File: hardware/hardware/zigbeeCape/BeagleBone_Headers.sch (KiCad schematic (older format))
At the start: 2 parts

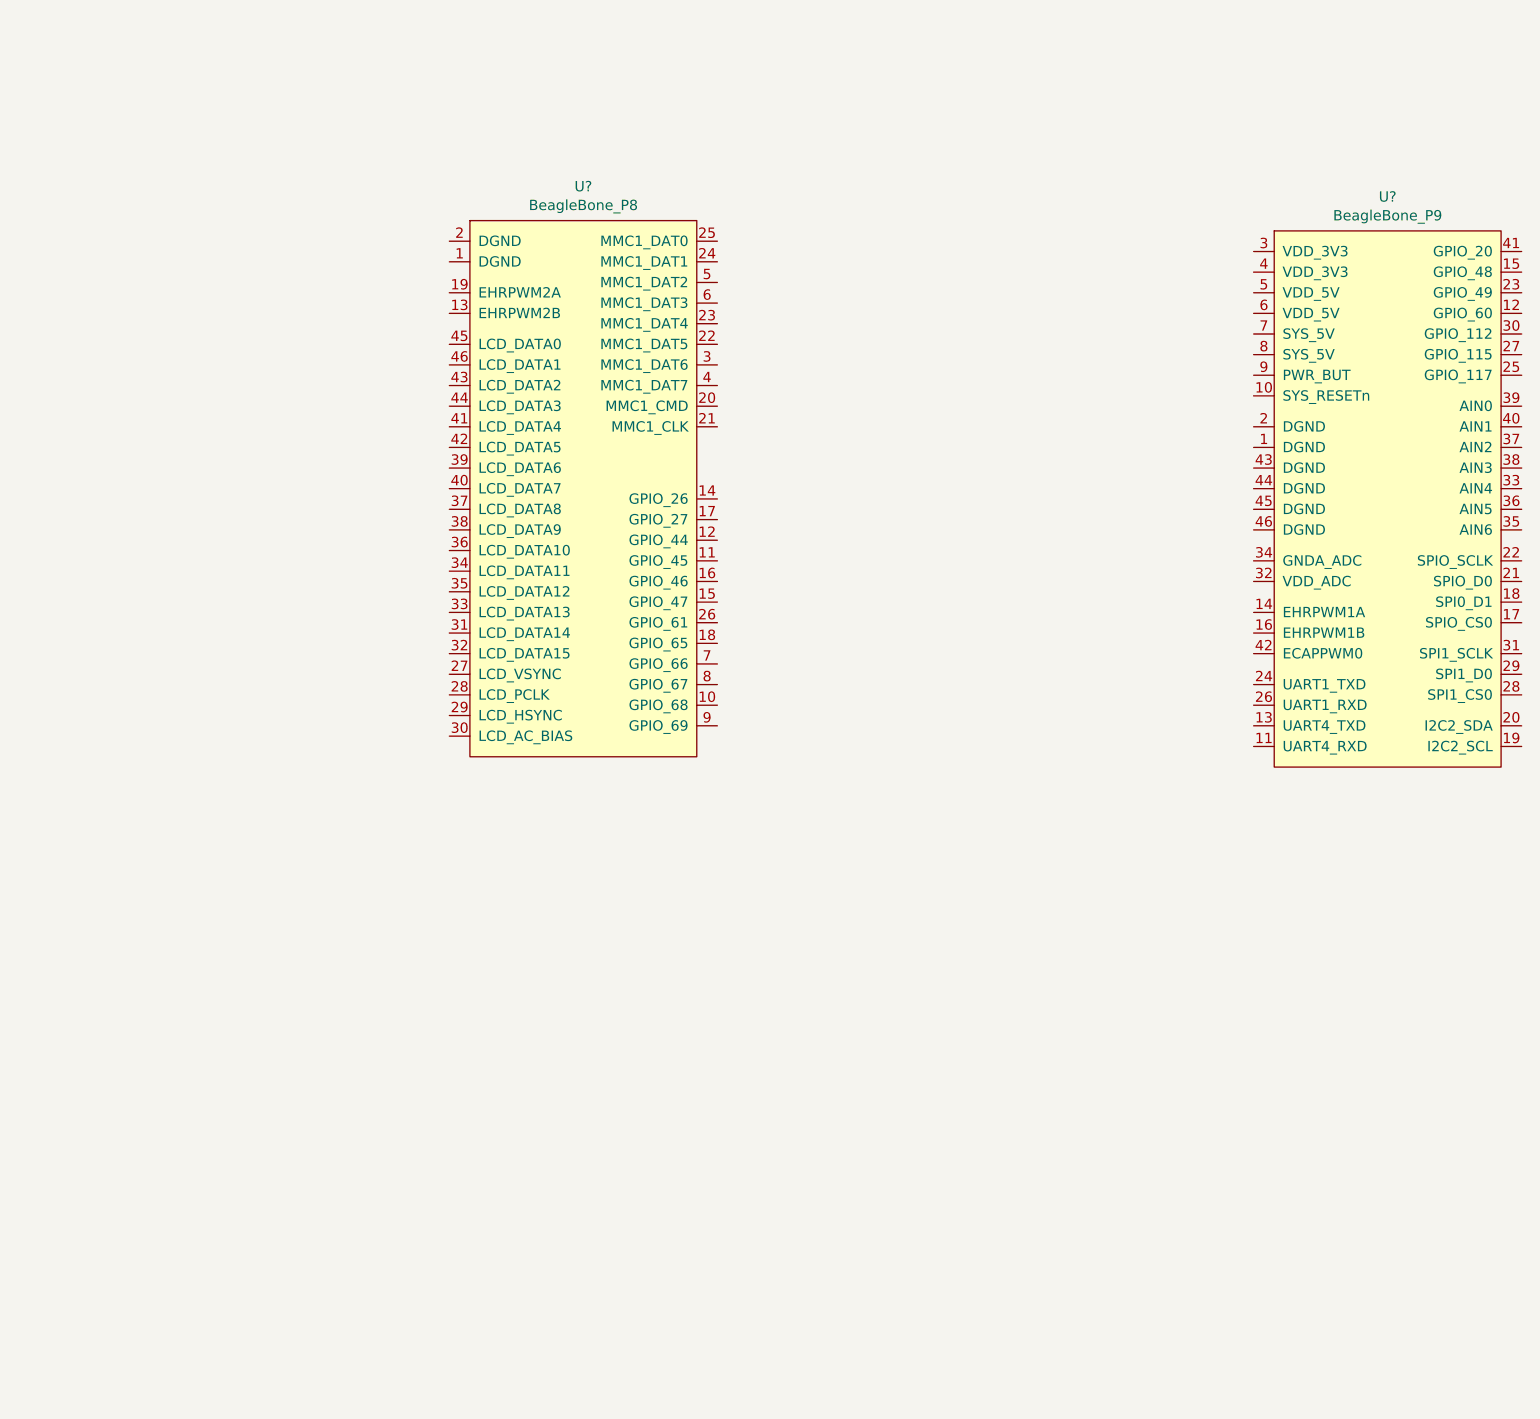
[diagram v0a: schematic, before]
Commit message: Added beaglebone header heiarcy pins
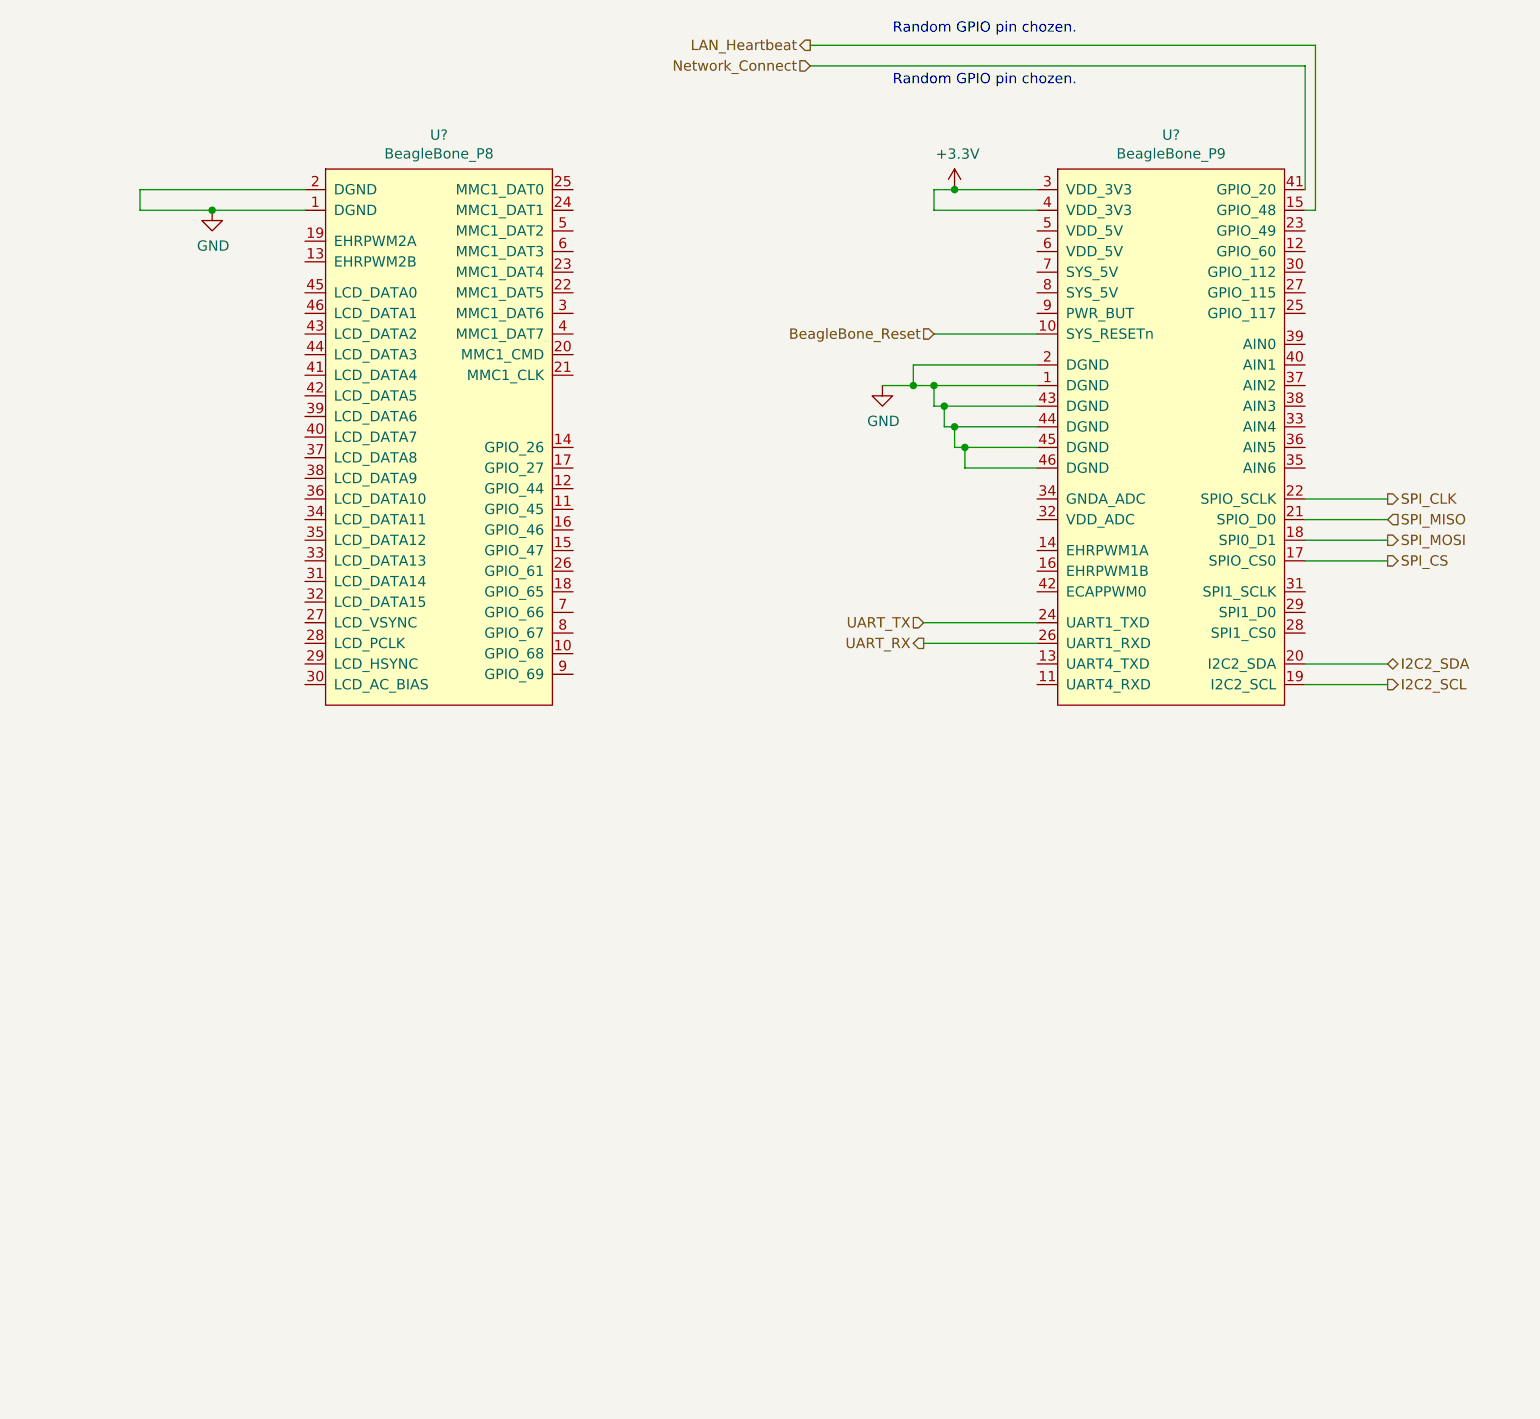
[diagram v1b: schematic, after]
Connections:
- net GND: now reaches U?.1 (DGND)
- net GND: now also U?.1 (DGND), U?.2 (DGND), U?.2 (DGND), U?.43 (DGND), U?.44 (DGND), U?.45 (DGND), U?.46 (DGND)
- net BeagleBone_Reset: now reaches U?.10 (SYS_RESETn)
- net LAN_Heartbeat: now reaches U?.15 (GPIO_48)
- net SPI_CS: now reaches U?.17 (SPIO_CS0)
- net SPI_MOSI: now reaches U?.18 (SPI0_D1)
- net I2C2_SCL: now reaches U?.19 (I2C2_SCL)
- net I2C2_SDA: now reaches U?.20 (I2C2_SDA)
- net SPI_MISO: now reaches U?.21 (SPIO_D0)
- net SPI_CLK: now reaches U?.22 (SPIO_SCLK)
- net UART_TX: now reaches U?.24 (UART1_TXD)
- net UART_RX: now reaches U?.26 (UART1_RXD)
- net +3V3: now reaches U?.3 (VDD_3V3)
- net +3V3: now also U?.4 (VDD_3V3)
- net Network_Connect: now reaches U?.41 (GPIO_20)
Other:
- note added: "Random GPIO pin chozen."
- moved on the sheet: U?
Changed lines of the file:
@@
 L BeagleBone:BeagleBone_P8 U?
 U 1 1 609FD186
-P 3600 4300
-F 0 "U?" H 3600 7065 50  0000 C CNN
-F 1 "BeagleBone_P8" H 3600 6974 50  0000 C CNN
-F 2 "" H 4200 7050 50  0001 C CNN
-F 3 "" H 4200 7050 50  0001 C CNN
-	1    3600 4300
+P 2900 4050
+F 0 "U?" H 2900 6815 50  0000 C CNN
+F 1 "BeagleBone_P8" H 2900 6724 50  0000 C CNN
+F 2 "" H 3500 6800 50  0001 C CNN
+F 3 "" H 3500 6800 50  0001 C CNN
+	1    2900 4050
 	1    0    0    -1
 $EndComp
@@
 L BeagleBone:BeagleBone_P9 U?
 U 1 1 609FDC70
-P 7500 4350
-F 0 "U?" H 7500 7115 50  0000 C CNN
-F 1 "BeagleBone_P9" H 7500 7024 50  0000 C CNN
-F 2 "" H 7000 7000 50  0001 C CNN
-F 3 "" H 7000 7000 50  0001 C CNN
-	1    7500 4350
+P 6450 4050
+F 0 "U?" H 6450 6815 50  0000 C CNN
+F 1 "BeagleBone_P9" H 6450 6724 50  0000 C CNN
+F 2 "" H 5950 6700 50  0001 C CNN
+F 3 "" H 5950 6700 50  0001 C CNN
+	1    6450 4050
 	1    0    0    -1
 $EndComp
+Text HLabel 5300 2250 0    50   Input ~ 0
+BeagleBone_Reset
+Text HLabel 4700 850  0    50   Output ~ 0
+LAN_Heartbeat
+Text HLabel 4700 950  0    50   Input ~ 0
+Network_Connect
+Text HLabel 5250 3650 0    50   Input ~ 0
+UART_TX
+Text HLabel 7500 3150 2    50   Input ~ 0
+SPI_MISO
+Text HLabel 7500 3250 2    50   Output ~ 0
+SPI_MOSI
+Text HLabel 7500 3350 2    50   Output ~ 0
+SPI_CS
+Text HLabel 7500 3050 2    50   Output ~ 0
+SPI_CLK
+Text HLabel 7500 3950 2    50   Output ~ 0
+I2C2_SCL
+Text HLabel 7500 3850 2    50   BiDi ~ 0
+I2C2_SDA
+Wire Wire Line
+	5800 2250 5300 2250
+Text HLabel 5250 3750 0    50   Output ~ 0
+UART_RX
+Wire Wire Line
+	5800 3750 5250 3750
+Wire Wire Line
+	5250 3650 5800 3650
+Wire Wire Line
+	7100 3950 7500 3950
+Wire Wire Line
+	7500 3850 7100 3850
+Wire Wire Line
+	7500 3350 7100 3350
+Wire Wire Line
+	7100 3250 7500 3250
+Wire Wire Line
+	7500 3150 7100 3150
+Wire Wire Line
+	7500 3050 7100 3050
+Wire Wire Line
+	4700 950  7100 950
+Wire Wire Line
+	7100 950  7100 1550
+Wire Wire Line
+	4700 850  7150 850
+Wire Wire Line
+	7150 850  7150 1650
+Wire Wire Line
+	7150 1650 7100 1650
+Text Notes 5100 800  0    50   ~ 0
+Random GPIO pin chozen.
+Text Notes 5100 1050 0    50   ~ 0
+Random GPIO pin chozen.
+Wire Wire Line
+	2250 1650 1800 1650
+Wire Wire Line
+	2250 1550 1450 1550
+Wire Wire Line
+	1450 1550 1450 1650
+Wire Wire Line
+	5800 1550 5400 1550
+Wire Wire Line
+	5800 1650 5300 1650
+Wire Wire Line
+	5300 1550 5300 1650
+Wire Wire Line
+	5800 2400 5200 2400
+Wire Wire Line
+	5200 2400 5200 2500
+Wire Wire Line
+	5800 2500 5300 2500
+Connection ~ 5200 2500
+Wire Wire Line
+	5200 2500 5050 2500
+Wire Wire Line
+	5800 2600 5350 2600
+Wire Wire Line
+	5300 2600 5300 2500
+Connection ~ 5300 2500
+Wire Wire Line
+	5300 2500 5200 2500
+Wire Wire Line
+	5800 2700 5400 2700
+Wire Wire Line
+	5350 2700 5350 2600
+Connection ~ 5350 2600
+Wire Wire Line
+	5350 2600 5300 2600
+Wire Wire Line
+	5800 2800 5450 2800
+Wire Wire Line
+	5400 2800 5400 2700
+Connection ~ 5400 2700
+Wire Wire Line
+	5400 2700 5350 2700
+Wire Wire Line
+	5800 2900 5450 2900
+Wire Wire Line
+	5450 2900 5450 2800
+Connection ~ 5450 2800
+Wire Wire Line
+	5450 2800 5400 2800
+$Comp
+L power:GND #PWR?
+U 1 1 608F7A9D
+P 1800 1650
+F 0 "#PWR?" H 1800 1400 50  0001 C CNN
+F 1 "GND" H 1805 1477 50  0000 C CNN
+F 2 "" H 1800 1650 50  0001 C CNN
+F 3 "" H 1800 1650 50  0001 C CNN
+	1    1800 1650
+	1    0    0    -1
+$EndComp
+Connection ~ 1800 1650
+Wire Wire Line
+	1800 1650 1450 1650
+$Comp
+L power:GND #PWR?
+U 1 1 608F7F64
+P 5050 2500
+F 0 "#PWR?" H 5050 2250 50  0001 C CNN
+F 1 "GND" H 5055 2327 50  0000 C CNN
+F 2 "" H 5050 2500 50  0001 C CNN
+F 3 "" H 5050 2500 50  0001 C CNN
+	1    5050 2500
+	1    0    0    -1
+$EndComp
+$Comp
+L power:+3.3V #PWR?
+U 1 1 608FAB4C
+P 5400 1550
+F 0 "#PWR?" H 5400 1400 50  0001 C CNN
+F 1 "+3.3V" H 5415 1723 50  0000 C CNN
+F 2 "" H 5400 1550 50  0001 C CNN
+F 3 "" H 5400 1550 50  0001 C CNN
+	1    5400 1550
+	1    0    0    -1
+$EndComp
+Connection ~ 5400 1550
+Wire Wire Line
+	5400 1550 5300 1550
 $EndSCHEMATC

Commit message: Assigned Pin types, cleaned stuff up, Fixed most errors from the DRC (questions on the last few)
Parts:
- gave numbers to parts that had none: 2
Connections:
- no-connect marks 0 -> 71
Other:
- note added: "BeagleBone Headers"
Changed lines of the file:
@@
 $EndDescr
 $Comp
-L BeagleBone:BeagleBone_P8 U?
+L BeagleBone:BeagleBone_P8 U4
 U 1 1 609FD186
 P 2900 4050
-F 0 "U?" H 2900 6815 50  0000 C CNN
+F 0 "U4" H 2900 6815 50  0000 C CNN
 F 1 "BeagleBone_P8" H 2900 6724 50  0000 C CNN
 F 2 "" H 3500 6800 50  0001 C CNN
@@
 $EndComp
 $Comp
-L BeagleBone:BeagleBone_P9 U?
+L BeagleBone:BeagleBone_P9 U5
 U 1 1 609FDC70
 P 6450 4050
-F 0 "U?" H 6450 6815 50  0000 C CNN
+F 0 "U5" H 6450 6815 50  0000 C CNN
 F 1 "BeagleBone_P9" H 6450 6724 50  0000 C CNN
 F 2 "" H 5950 6700 50  0001 C CNN
@@
 	5450 2800 5400 2800
 $Comp
-L power:GND #PWR?
+L power:GND #PWR046
 U 1 1 608F7A9D
 P 1800 1650
-F 0 "#PWR?" H 1800 1400 50  0001 C CNN
+F 0 "#PWR046" H 1800 1400 50  0001 C CNN
 F 1 "GND" H 1805 1477 50  0000 C CNN
 F 2 "" H 1800 1650 50  0001 C CNN
@@
 	1800 1650 1450 1650
 $Comp
-L power:GND #PWR?
+L power:GND #PWR047
 U 1 1 608F7F64
 P 5050 2500
-F 0 "#PWR?" H 5050 2250 50  0001 C CNN
+F 0 "#PWR047" H 5050 2250 50  0001 C CNN
 F 1 "GND" H 5055 2327 50  0000 C CNN
 F 2 "" H 5050 2500 50  0001 C CNN
@@
 $EndComp
 $Comp
-L power:+3.3V #PWR?
+L power:+3.3V #PWR048
 U 1 1 608FAB4C
 P 5400 1550
-F 0 "#PWR?" H 5400 1400 50  0001 C CNN
+F 0 "#PWR048" H 5400 1400 50  0001 C CNN
 F 1 "+3.3V" H 5415 1723 50  0000 C CNN
 F 2 "" H 5400 1550 50  0001 C CNN
@@
 Wire Wire Line
 	5400 1550 5300 1550
+NoConn ~ 5800 3500
+NoConn ~ 5800 3400
+NoConn ~ 5800 3300
+NoConn ~ 5800 3150
+NoConn ~ 5800 3050
+NoConn ~ 5800 3950
+NoConn ~ 5800 3850
+NoConn ~ 7100 3700
+NoConn ~ 7100 3600
+NoConn ~ 7100 3500
+NoConn ~ 7100 2900
+NoConn ~ 7100 2800
+NoConn ~ 7100 2700
+NoConn ~ 7100 2600
+NoConn ~ 7100 2500
+NoConn ~ 7100 2400
+NoConn ~ 7100 1750
+NoConn ~ 7100 1850
+NoConn ~ 7100 1950
+NoConn ~ 7100 2050
+NoConn ~ 7100 2150
+NoConn ~ 7100 2300
+NoConn ~ 5800 2150
+NoConn ~ 5800 2050
+NoConn ~ 5800 1950
+NoConn ~ 5800 1850
+NoConn ~ 5800 1750
+NoConn ~ 2250 3950
+NoConn ~ 2250 3850
+NoConn ~ 2250 3750
+NoConn ~ 2250 3650
+NoConn ~ 2250 3550
+NoConn ~ 2250 3450
+NoConn ~ 2250 3350
+NoConn ~ 2250 3250
+NoConn ~ 2250 3150
+NoConn ~ 2250 3050
+NoConn ~ 2250 2950
+NoConn ~ 2250 2850
+NoConn ~ 2250 2750
+NoConn ~ 2250 2650
+NoConn ~ 2250 2550
+NoConn ~ 2250 2450
+NoConn ~ 2250 2350
+NoConn ~ 2250 2250
+NoConn ~ 2250 2150
+NoConn ~ 3550 2800
+NoConn ~ 3550 2900
+NoConn ~ 3550 3000
+NoConn ~ 3550 3100
+NoConn ~ 3550 3200
+NoConn ~ 3550 3300
+NoConn ~ 3550 3400
+NoConn ~ 3550 3500
+NoConn ~ 3550 3600
+NoConn ~ 3550 3700
+NoConn ~ 3550 3800
+NoConn ~ 3550 3900
+NoConn ~ 3550 2450
+NoConn ~ 3550 2350
+NoConn ~ 3550 2250
+NoConn ~ 3550 2150
+NoConn ~ 3550 2050
+NoConn ~ 3550 1550
+NoConn ~ 3550 1650
+NoConn ~ 3550 1750
+NoConn ~ 3550 1850
+NoConn ~ 3550 1950
+NoConn ~ 2250 2050
+NoConn ~ 2250 1900
+NoConn ~ 2250 1800
+Text Notes 850  7300 0    295  ~ 59
+BeagleBone Headers
 $EndSCHEMATC

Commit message: Fixed a few little things
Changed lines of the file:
@@
 Wire Wire Line
 	7500 3050 7100 3050
-Wire Wire Line
-	4700 950  7100 950
-Wire Wire Line
-	7100 950  7100 1550
-Wire Wire Line
-	4700 850  7150 850
-Wire Wire Line
-	7150 850  7150 1650
-Wire Wire Line
-	7150 1650 7100 1650
 Text Notes 5100 800  0    50   ~ 0
 Random GPIO pin chozen.
@@
 Random GPIO pin chozen.
 Wire Wire Line
-	2250 1650 1800 1650
-Wire Wire Line
 	2250 1550 1450 1550
 Wire Wire Line
 	1450 1550 1450 1650
-Wire Wire Line
-	5800 1550 5400 1550
 Wire Wire Line
 	5800 1650 5300 1650
@@
 Wire Wire Line
 	5200 2400 5200 2500
-Wire Wire Line
-	5800 2500 5300 2500
 Connection ~ 5200 2500
-Wire Wire Line
-	5200 2500 5050 2500
-Wire Wire Line
-	5800 2600 5350 2600
-Wire Wire Line
-	5300 2600 5300 2500
-Connection ~ 5300 2500
-Wire Wire Line
-	5300 2500 5200 2500
-Wire Wire Line
-	5800 2700 5400 2700
-Wire Wire Line
-	5350 2700 5350 2600
-Connection ~ 5350 2600
-Wire Wire Line
-	5350 2600 5300 2600
-Wire Wire Line
-	5800 2800 5450 2800
-Wire Wire Line
-	5400 2800 5400 2700
-Connection ~ 5400 2700
-Wire Wire Line
-	5400 2700 5350 2700
-Wire Wire Line
-	5800 2900 5450 2900
-Wire Wire Line
-	5450 2900 5450 2800
-Connection ~ 5450 2800
-Wire Wire Line
-	5450 2800 5400 2800
 $Comp
 L power:GND #PWR046
 U 1 1 608F7A9D
-P 1800 1650
-F 0 "#PWR046" H 1800 1400 50  0001 C CNN
-F 1 "GND" H 1805 1477 50  0000 C CNN
-F 2 "" H 1800 1650 50  0001 C CNN
-F 3 "" H 1800 1650 50  0001 C CNN
-	1    1800 1650
+P 1450 1800
+F 0 "#PWR046" H 1450 1550 50  0001 C CNN
+F 1 "GND" H 1455 1627 50  0000 C CNN
+F 2 "" H 1450 1800 50  0001 C CNN
+F 3 "" H 1450 1800 50  0001 C CNN
+	1    1450 1800
 	1    0    0    -1
 $EndComp
-Connection ~ 1800 1650
-Wire Wire Line
-	1800 1650 1450 1650
 $Comp
 L power:GND #PWR047
 U 1 1 608F7F64
-P 5050 2500
-F 0 "#PWR047" H 5050 2250 50  0001 C CNN
-F 1 "GND" H 5055 2327 50  0000 C CNN
-F 2 "" H 5050 2500 50  0001 C CNN
-F 3 "" H 5050 2500 50  0001 C CNN
-	1    5050 2500
+P 4800 2550
+F 0 "#PWR047" H 4800 2300 50  0001 C CNN
+F 1 "GND" H 4805 2377 50  0000 C CNN
+F 2 "" H 4800 2550 50  0001 C CNN
+F 3 "" H 4800 2550 50  0001 C CNN
+	1    4800 2550
 	1    0    0    -1
 $EndComp
@@
 L power:+3.3V #PWR048
 U 1 1 608FAB4C
-P 5400 1550
-F 0 "#PWR048" H 5400 1400 50  0001 C CNN
-F 1 "+3.3V" H 5415 1723 50  0000 C CNN
-F 2 "" H 5400 1550 50  0001 C CNN
-F 3 "" H 5400 1550 50  0001 C CNN
-	1    5400 1550
+P 5300 1500
+F 0 "#PWR048" H 5300 1350 50  0001 C CNN
+F 1 "+3.3V" H 5315 1673 50  0000 C CNN
+F 2 "" H 5300 1500 50  0001 C CNN
+F 3 "" H 5300 1500 50  0001 C CNN
+	1    5300 1500
 	1    0    0    -1
 $EndComp
-Connection ~ 5400 1550
-Wire Wire Line
-	5400 1550 5300 1550
 NoConn ~ 5800 3500
 NoConn ~ 5800 3400
@@
 Text Notes 850  7300 0    295  ~ 59
 BeagleBone Headers
+Wire Wire Line
+	5300 1550 5800 1550
+Wire Wire Line
+	5300 1500 5300 1550
+Connection ~ 5300 1550
+Wire Wire Line
+	5200 2500 5800 2500
+Wire Wire Line
+	5800 2900 5200 2900
+Wire Wire Line
+	5200 2900 5200 2800
+Wire Wire Line
+	5800 2800 5200 2800
+Connection ~ 5200 2800
+Wire Wire Line
+	5200 2800 5200 2700
+Wire Wire Line
+	5800 2700 5200 2700
+Connection ~ 5200 2700
+Wire Wire Line
+	5200 2700 5200 2600
+Wire Wire Line
+	5800 2600 5200 2600
+Connection ~ 5200 2600
+Wire Wire Line
+	5200 2600 5200 2500
+Wire Wire Line
+	5200 2400 4800 2400
+Wire Wire Line
+	4800 2400 4800 2550
+Connection ~ 5200 2400
+Wire Wire Line
+	7350 1650 7350 850
+Wire Wire Line
+	4700 850  7350 850
+Wire Wire Line
+	7100 1650 7350 1650
+Wire Wire Line
+	7100 1550 7250 1550
+Wire Wire Line
+	7250 1550 7250 950
+Wire Wire Line
+	4700 950  7250 950
+Wire Wire Line
+	1450 1650 1450 1800
+Wire Wire Line
+	1450 1650 2250 1650
+Connection ~ 1450 1650
 $EndSCHEMATC
